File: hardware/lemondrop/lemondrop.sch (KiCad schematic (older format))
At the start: 30 parts

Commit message: MAX5864 basics in schematic
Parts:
- added C? (x3): 330nF, symbol C
- added C? (x4): 100nF, symbol C
- added C? (x4): 2.2μF, symbol C
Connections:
- net labels added: CLK, CS_AD, CS_XCVR, DA0, DA1, DA2, DA3, DA4, DA5, DA6, DA7, DA8, DA9, DD2, DD3, DD4, DD5, DD6, DD7, DD8, DD9
- net labels removed: CS
- wire segments 98 -> 188

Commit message: more MAX2837 stuff in schematic
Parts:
- removed T? (x2): TRANSFO, symbol TRANSFO
- added C? (x2): 22pF, symbol C
- added C? (x2): 3pF, symbol C
- added T? (x2): BALUN, symbol BALUN
- C? (x5): value C -> 22pF
- C? (x5): value C -> 10nF
- C?: value C -> 100pF
- C?: value C -> 100nF
- L?: value INDUCTOR -> 6.2nH
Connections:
- wire segments 188 -> 154
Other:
- moved on the sheet: C?, L?, R?, U?

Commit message: more schematic details
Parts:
- added C?: 1nF, symbol C
- added C?: DNP, symbol C
- added C? (x4): 100nF, symbol C
- added C? (x3): 2.2μF, symbol C
- added C? (x4): 22pF, symbol C
- added P? (x2): GSG-SMA-CONN, symbol GSG-SMA-CONN
- C?: value C -> 180pF
- C?: value C -> 3.3nF
- R? (x2): value R -> 475
- R? (x4): value R -> 1k
- R? (x4): value R -> 4k7
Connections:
- net GND: now also C?.1, C?.2, C?.2, C?.2, C?.2, C?.2, C?.2, C?.2, C?.2, C?.2, C?.2, C?.2, P?.2 (GND), P?.2 (GND), P?.3 (GND), P?.3 (GND), P?.4 (GND), P?.4 (GND), P?.5 (GND), P?.5 (GND)
- net VCC: now also C?.1, C?.1, C?.1, C?.1, C?.1, C?.1, C?.1
- net XTAL2: now reaches U?.17 (XTAL2)
- net XTAL2: now also C?.2
- net at U?.10 (QA+), U?.35 (RXBBQ-): now also C?.1
- net at U?.36 (RXBBQ+), U?.9 (QA-): now also C?.1
- net at U?.37 (RXBBI-), U?.4 (IA-): now also C?.1
- net at U?.3 (IA+), U?.38 (RXBBI+): now also C?.1
- net at C?.2: now also P?.1 (RF)
- net at T?.1 (S1): now also P?.1 (RF)
- new net XCVR_CLK: C?.1, C?.2
- no-connect marks 0 -> 1
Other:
- moved on the sheet: C?, L?, R?, T?, U?

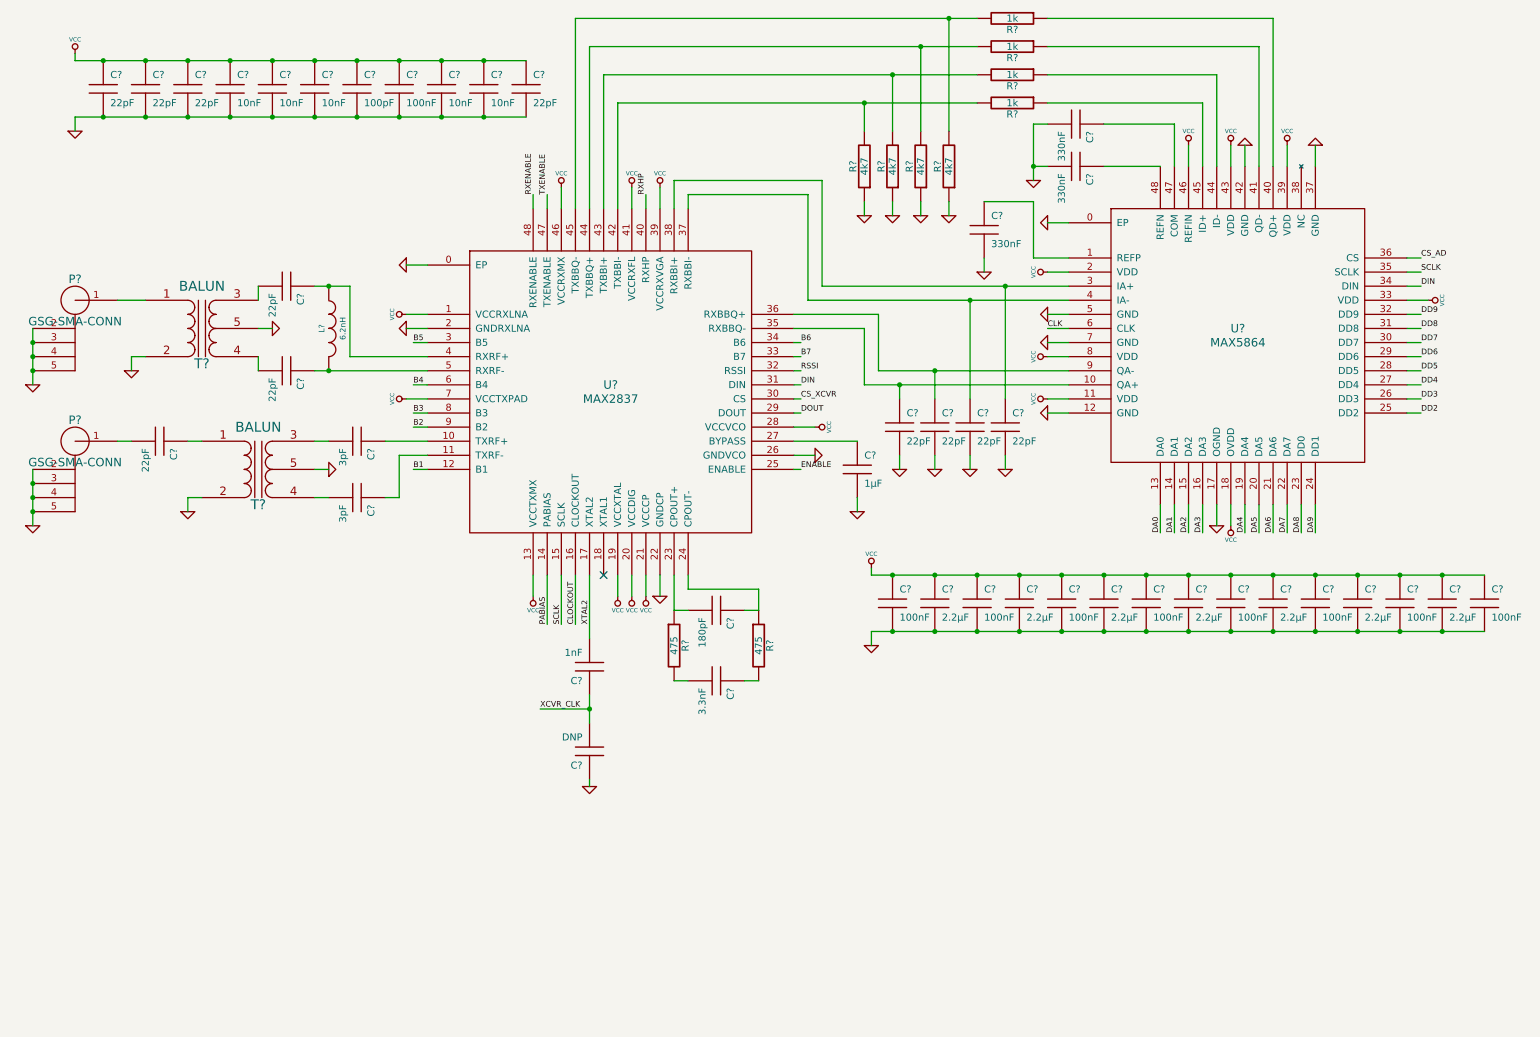
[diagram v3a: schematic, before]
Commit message: added Si5351C clock generator
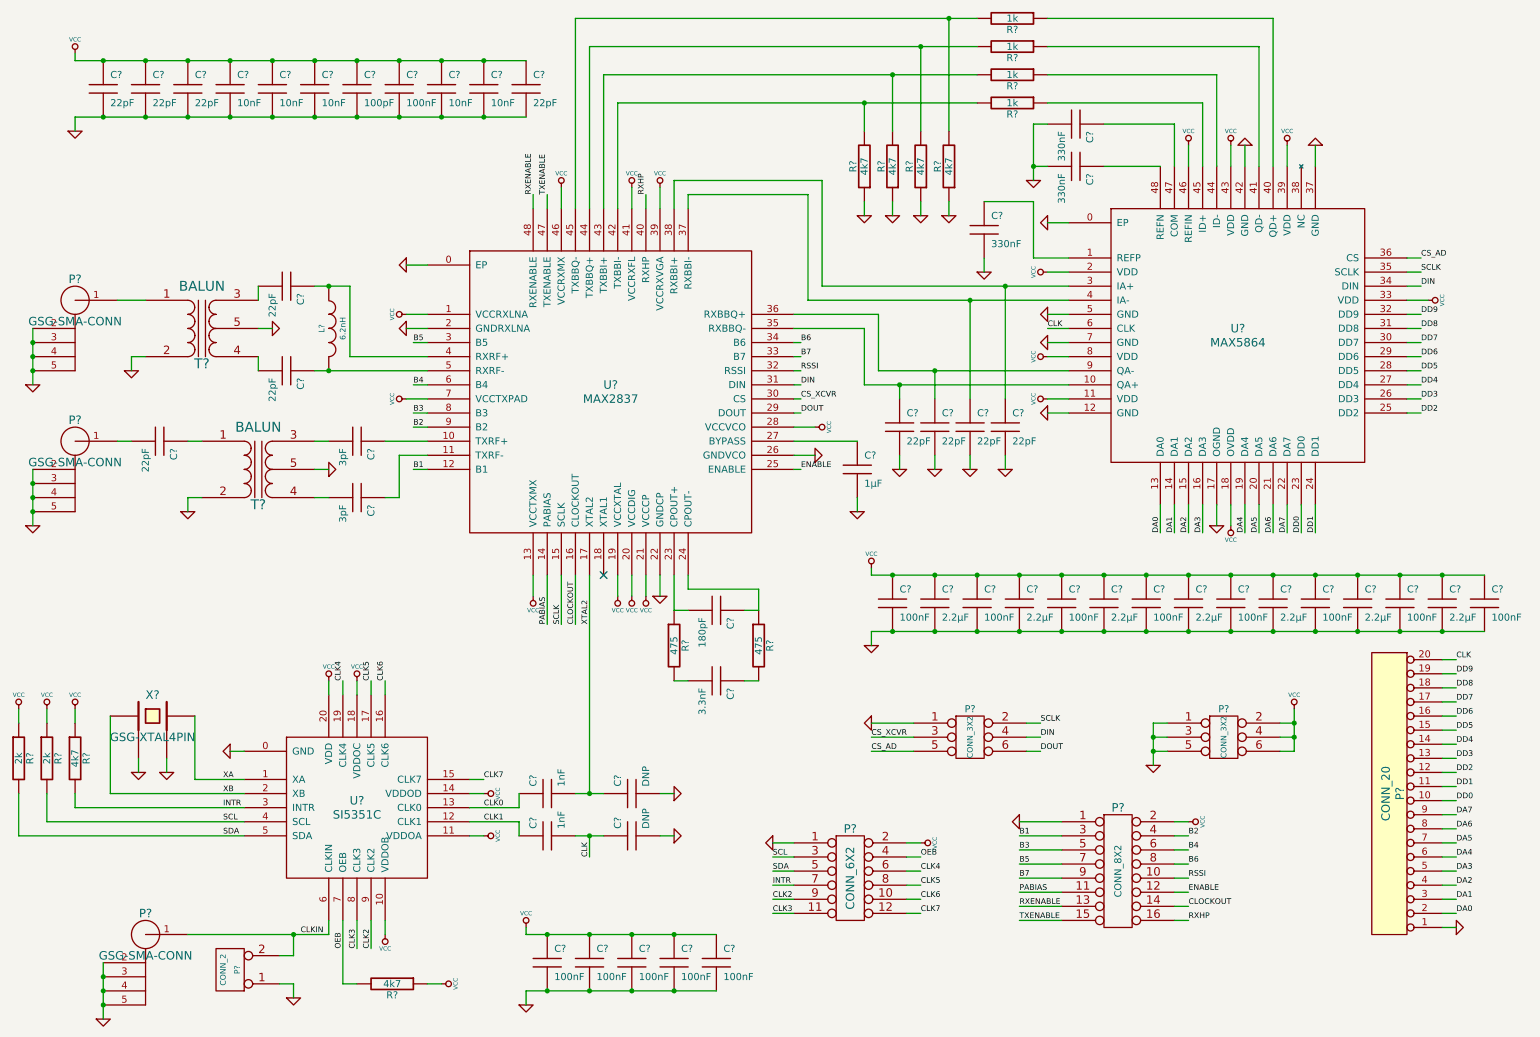
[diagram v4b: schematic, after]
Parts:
- added C? (x5): 100nF, symbol C
- added C?: DNP, symbol C
- added C?: 1nF, symbol C
- added P?: GSG-SMA-CONN, symbol GSG-SMA-CONN
- added P?: CONN_2, symbol CONN_2
- added P?: CONN_20, symbol CONN_20
- added P?: CONN_6X2, symbol CONN_6X2
- added P? (x2): CONN_3X2, symbol CONN_3X2
- added P?: CONN_8X2, symbol CONN_8X2
- added R? (x2): 4k7, symbol R
- added R? (x2): 2k, symbol R
- added U?: SI5351C, symbol SI5351C
- added X?: GSG-XTAL4PIN, symbol GSG-XTAL4PIN
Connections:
- net B1: now also P?.3
- net B2: now also P?.4
- net B3: now also P?.5
- net B4: now also P?.6
- net B5: now also P?.7
- net B6: now also P?.8
- net B7: now also P?.9
- net CLK: now also C?.1, C?.2, P?.20 (P20)
- net CLOCKOUT: now also P?.14
- net CS_AD: now also P?.5
- net CS_XCVR: now also P?.3
- net DA0: now also P?.2 (P2)
- net DA1: now also P?.3 (P3)
- net DA2: now also P?.4 (P4)
- net DA3: now also P?.5 (P5)
- net DA4: now also P?.6 (P6)
- net DA5: now also P?.7 (P7)
- net DA6: now also P?.8 (P8)
- net DA7: now also P?.9 (P9)
- net DD2: now also P?.12 (P12)
- net DD3: now also P?.13 (P13)
- net DD4: now also P?.14 (P14)
- net DD5: now also P?.15 (P15)
- net DD6: now also P?.16 (P16)
- net DD7: now also P?.17 (P17)
- net DD8: now also P?.18 (P18)
- net DD9: now also P?.19 (P19)
- net DIN: now also P?.4
- net DOUT: now also P?.6
- net ENABLE: now also P?.12
- net GND: now also C?.2, C?.2, C?.2, C?.2, C?.2, C?.2, C?.2, P?.1, P?.1, P?.1, P?.1 (P1), P?.1 (P1), P?.1 (P1), P?.2 (GND), P?.3, P?.3 (GND), P?.4 (GND), P?.5, P?.5 (GND), U?.0 (GND), X?.2, X?.4; no longer C?.1
- net PABIAS: now also P?.11
- net RSSI: now also P?.10
- net RXENABLE: now also P?.13
- net RXHP: now also P?.16
- net SCLK: now also P?.2
- net TXENABLE: now also P?.15
- net VCC: now also C?.1, C?.1, C?.1, C?.1, C?.1, P?.2, P?.2, P?.2 (P2), P?.4, P?.6, R?.1, R?.1, R?.1, R?.1, U?.10 (VDDOB), U?.11 (VDDOA), U?.14 (VDDOD), U?.18 (VDDOC), U?.20 (VDD)
- net XTAL2: now also C?.1
- net DA8 renamed DD0
- net DD0: now also P?.10 (P10)
- net DA9 renamed DD1
- net DD1: now also P?.11 (P11)
- net XCVR_CLK renamed CLK0
- net CLK0: now also U?.13 (CLK0); no longer C?.2
- new net CLK1: C?.1, U?.12 (CLK1)
- new net CLK2: P?.9, U?.9 (CLK2)
- new net CLK3: P?.11, U?.8 (CLK3)
- new net CLK4: P?.6 (P6), U?.19 (CLK4)
- new net CLK5: P?.8 (P8), U?.17 (CLK5)
- new net CLK6: P?.10, U?.16 (CLK6)
- new net CLK7: P?.12, U?.15 (CLK7)
- new net CLKIN: P?.1 (RF), P?.2 (PM), U?.6 (CLKIN)
- new net INTR: P?.7 (P7), R?.2, U?.3 (INTR)
- new net OEB: P?.4 (P4), R?.2, U?.7 (OEB)
- new net SCL: P?.3 (P3), R?.2, U?.4 (SCL)
- new net SDA: P?.5 (P5), R?.2, U?.5 (SDA)
- new net XA: U?.1 (XA), X?.3
- new net XB: U?.2 (XB), X?.1
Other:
- moved on the sheet: C?

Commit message: annotated schematic
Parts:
- gave numbers to parts that had none: 80

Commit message: various fixes and suggestions from Jared
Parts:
- removed P5: CONN_20, symbol CONN_20
- added C51, C52, C53, C54: 22pF, symbol C
- added L2, L3, L4: DNP, symbol INDUCTOR
- added P5: CONN_20X2, symbol CONN_20X2
- added R15, R16, R17, R18, R35: 0, symbol R
- added R19: 4k7, symbol R
- added R20, R21, R22, R23, R24, R25, R26, R27, R28, R29, R30, R31, R32, R33, R34: 100, symbol R
- added R36: DNP, symbol R
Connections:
- net CLK: now also R20.1
- net CLK2: now also R28.2; no longer P7.9
- net CLK3: now also R31.2; no longer P7.11
- net CLK4: now also R24.1; no longer P7.6 (P6)
- net CLK5: now also R26.1; no longer P7.8 (P8)
- net CLK6: now also R29.1; no longer P7.10
- net CLK7: now also R32.1; no longer P7.12
- net CLKIN: now also R35.1, R36.2; no longer P8.1 (RF)
- net DA0: now also R34.1
- net DA1: now also R33.1
- net DA2: now also R30.1
- net DA3: now also R27.1
- net DA4: now also R25.1
- net DA5: now also R23.1
- net DA6: now also R22.1
- net DA7: now also R21.1
- net DD0: now also P5.19 (P19)
- net DD1: now also P5.21 (P21)
- net DD2: now also P5.23 (P23)
- net DD3: now also P5.25
- net DD4: now also P5.27 (P27)
- net DD5: now also P5.29 (P29)
- net DD6: now also P5.31 (P31)
- net DD7: now also P5.33 (P33)
- net DD8: now also P5.35 (P35)
- net DD9: now also P5.37 (P37)
- net ENABLE: now also R19.1
- net GND: now also P5.1 (P1), P5.10 (P10), P5.12 (P12), P5.14 (P14), P5.16 (P16), P5.18 (P18), P5.2 (P2), P5.20 (P20), P5.22 (P22), P5.24 (P24), P5.26 (P26), P5.28 (P28), P5.30 (P30), P5.32 (P32), P5.34 (P34), P5.36 (P36), P5.38 (P38), P5.4 (P4), P5.40 (P40), P5.6 (P6), P5.8 (P8), R19.2, R36.1
- net at C22.1, U2.10 (TXRF+): now also L4.1
- net at C24.1, U2.11 (TXRF-): now also L4.2
- net at C17.1, U1.10 (QA+): now also C54.2, R18.1; no longer U2.35 (RXBBQ-)
- net at C18.1, U1.9 (QA-): now also C54.1, R17.1; no longer U2.36 (RXBBQ+)
- net at C19.1, U1.4 (IA-): now also C53.2, R16.1; no longer U2.37 (RXBBI-)
- net at C20.1, U1.3 (IA+): now also C53.1, R15.1; no longer U2.38 (RXBBI+)
- net at R1.1, U1.40 (QD+): now also C51.2
- net at R2.1, U1.41 (QD-): now also C51.1
- net at R3.1, U1.44 (ID-): now also C52.2
- net at R4.1, U1.45 (ID+): now also C52.1
- net at C15.2, T1.3 (PR2): now also L2.1
- net at C16.2, T1.4 (PR1): now also L2.2
- net at C24.2, T2.4 (PR1): now also L3.2
- net at C22.2, T2.3 (PR2): now also L3.1
- new net: R18.2, U2.35 (RXBBQ-)
- new net: R17.2, U2.36 (RXBBQ+)
- new net: R16.2, U2.37 (RXBBI-)
- new net: R15.2, U2.38 (RXBBI+)
- new net: P8.1 (RF), R35.2
- new net: P7.10, R29.2
- new net: P7.11, R31.1
- new net: P7.12, R32.2
- new net: P7.6 (P6), R24.2
- new net: P7.8 (P8), R26.2
- new net: P7.9, R28.1
- new net: P5.11 (P11), R25.2
- new net: P5.13 (P13), R23.2
- new net: P5.15 (P15), R22.2
- new net: P5.17 (P17), R21.2
- new net: P5.3 (P3), R34.2
- new net: P5.39 (P39), R20.2
- new net: P5.5 (P5), R33.2
- new net: P5.7 (P7), R30.2
- new net: P5.9 (P9), R27.2
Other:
- moved on the sheet: C1, C10, C11, C12, C13, C14, C15, C16, C17, C18, C19, C2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
